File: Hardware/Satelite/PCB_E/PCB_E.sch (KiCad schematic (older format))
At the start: 15 parts, among them J1 Conn_02x02_Counter_Clockwise, J12 Conector_Expansion_CanSat, J14 Conn_01x06, J15 Conn_01x06, J2 Conn_02x02_Counter_Clockwise, J3 Conn_02x02_Counter_Clockwise, J4 Conn_02x10_Odd_Even, J5 Conn_02x10_Odd_Even, J6 Conn_02x10_Odd_Even, J7 Conn_02x10_Odd_Even, J8 Conn_01x04, M1 Spacer, M2 Spacer, M3 Spacer

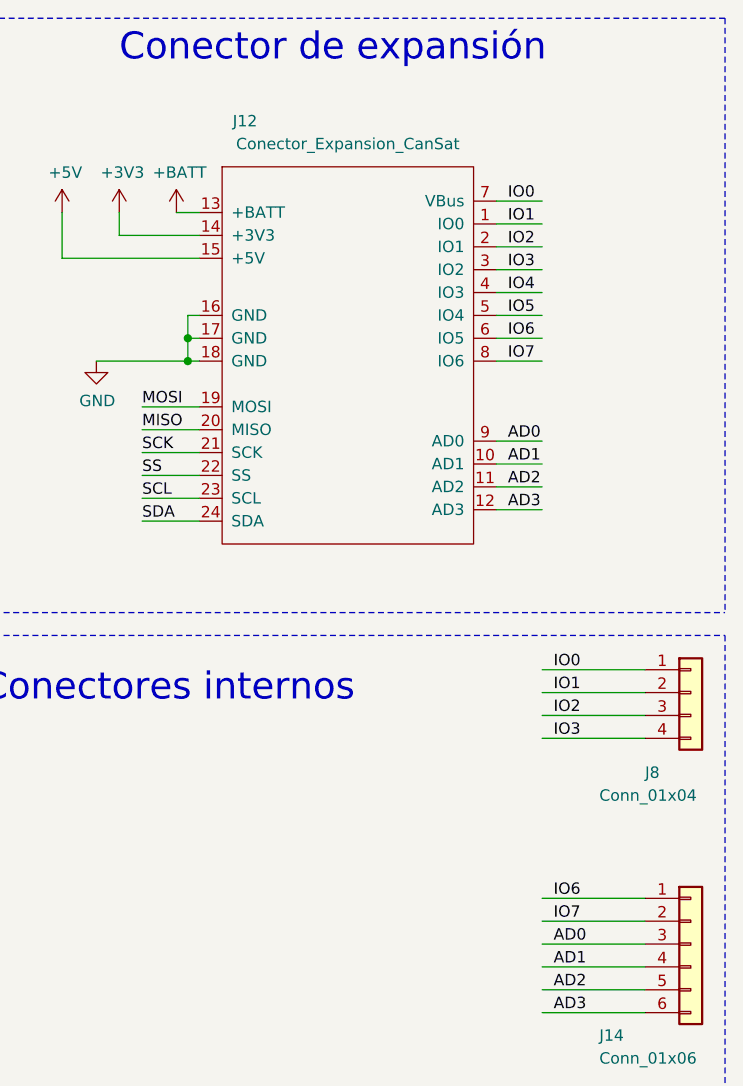
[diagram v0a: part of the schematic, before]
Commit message: Modificaciones D6 y serigrafia en PCB_E
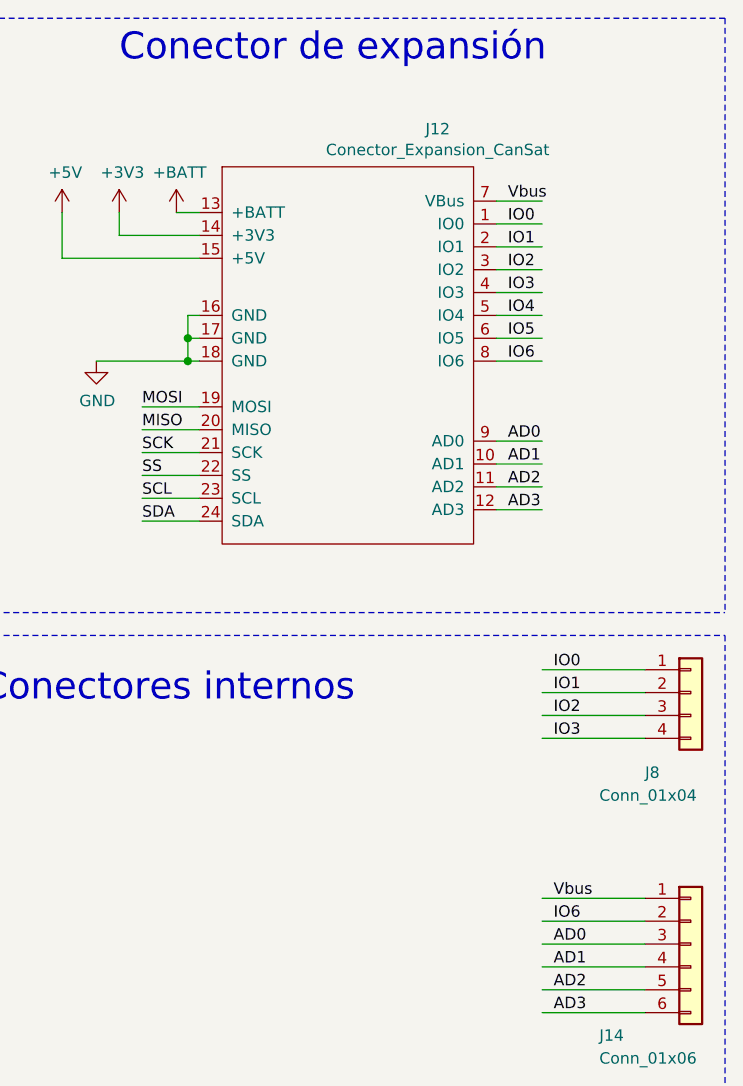
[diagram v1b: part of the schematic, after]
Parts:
- J12: Manufacturer Part Number SSQ-106-03-T-S -> (none); Quantity 4 -> (none)
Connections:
- net labels added: Vbus
- net labels removed: IO7
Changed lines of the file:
@@
 Text Label 9650 3900 0    50   ~ 0
 IO3
-Text Label 9450 2150 0    50   ~ 0
+Text Label 9450 2250 0    50   ~ 0
 IO6
 Wire Wire Line
@@
 Wire Wire Line
 	9600 5100 10050 5100
-Text Label 9450 2250 0    50   ~ 0
-IO7
+Text Label 9450 1550 0    50   ~ 0
+Vbus
 Text Label 9650 4800 0    50   ~ 0
 AD0
@@
 EndData
 $EndBitmap
-Text Label 9450 1550 0    50   ~ 0
+Text Label 9450 1650 0    50   ~ 0
 IO0
-Text Label 9450 1650 0    50   ~ 0
+Text Label 9450 1750 0    50   ~ 0
 IO1
-Text Label 9450 1750 0    50   ~ 0
+Text Label 9450 1850 0    50   ~ 0
 IO2
-Text Label 9450 1850 0    50   ~ 0
+Text Label 9450 1950 0    50   ~ 0
 IO3
-Text Label 9450 1950 0    50   ~ 0
+Text Label 9450 2050 0    50   ~ 0
 IO4
-Text Label 9450 2050 0    50   ~ 0
+Text Label 9450 2150 0    50   ~ 0
 IO5
 Text Label 9450 2600 0    50   ~ 0
@@
 Wire Wire Line
 	10050 4700 9600 4700
-Text Label 9650 4600 0    50   ~ 0
+Text Label 9650 4700 0    50   ~ 0
 IO6
-Text Label 9650 4700 0    50   ~ 0
-IO7
 $Comp
 L AXTEC_IC:MH_CanSat MH1
@@
 Text Notes 4450 4150 0    118  ~ 0
 Agujeros de montaje
-$Comp
-L AXTEC_IC:Conector_Expansion_CanSat J12
-U 1 1 5BC6ED70
-P 8750 2100
-F 0 "J12" H 8300 3000 50  0000 C CNN
-F 1 "Conector_Expansion_CanSat" H 8750 2900 50  0000 C CNN
-F 2 "AXTEC:Conector_Expansion_CanSat" H 8750 2600 50  0001 C CNN
-F 3 "" H 8750 2600 50  0001 C CNN
-F 4 "SSQ-106-03-T-S" H 8750 2100 50  0001 C CNN "Manufacturer Part Number"
-F 5 "4" H 8750 2100 50  0001 C CNN "Quantity"
-	1    8750 2100
-	1    0    0    -1
-$EndComp
 Wire Wire Line
 	8100 2950 7850 2950
@@
 	1    0    0    -1
 $EndComp
+$Comp
+L AXTEC_IC:Conector_Expansion_CanSat J12
+U 1 1 5C26BB39
+P 8750 2100
+F 0 "J12" H 9143 2965 50  0000 C CNN
+F 1 "Conector_Expansion_CanSat" H 9143 2874 50  0000 C CNN
+F 2 "AXTEC:Conector_Expansion_CanSat" H 8750 2600 50  0001 C CNN
+F 3 "" H 8750 2600 50  0001 C CNN
+	1    8750 2100
+	1    0    0    -1
+$EndComp
+Text Label 9650 4600 0    50   ~ 0
+Vbus
 $EndSCHEMATC

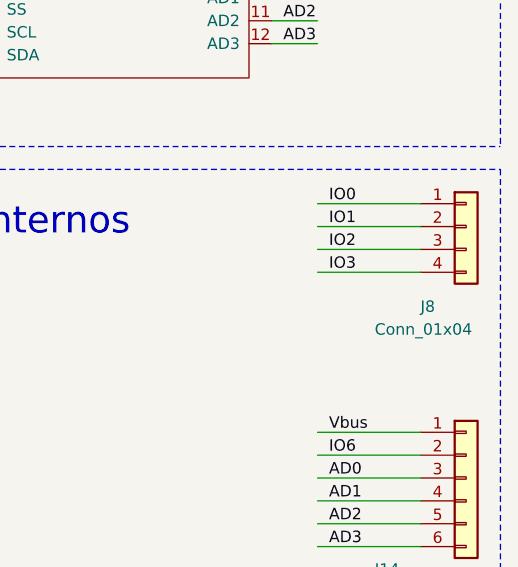
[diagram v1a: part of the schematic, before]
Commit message: Agregados pines faltantes en PCB_E
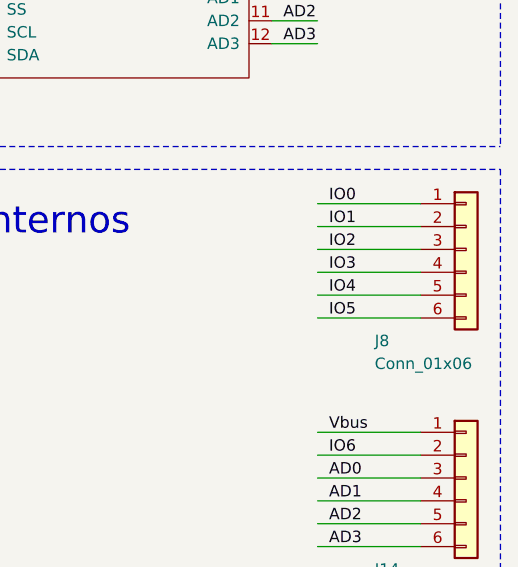
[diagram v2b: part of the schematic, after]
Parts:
- removed J8: Conn_01x04, Connector_PinHeader_2.54mm:PinHeader_1x04_P2.54mm_Vertical, symbol Connector_Generic:Conn_01x04
- added J8: Conn_01x06, Connector_PinHeader_2.54mm:PinHeader_1x06_P2.54mm_Vertical, symbol Connector_Generic:Conn_01x06
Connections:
- wire segments 75 -> 77
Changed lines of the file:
@@
-$EndComp
-$Comp
-L Connector_Generic:Conn_01x04 J8
-U 1 1 5BE3BD5B
-P 10250 3700
-F 0 "J8" H 10050 3350 50  0000 L CNN
-F 1 "Conn_01x04" H 9850 3250 50  0000 L CNN
-F 2 "Connector_PinHeader_2.54mm:PinHeader_1x04_P2.54mm_Vertical" H 10250 3700 50  0001 C CNN
-F 3 "~" H 10250 3700 50  0001 C CNN
-	1    10250 3700
-	1    0    0    -1
 $EndComp
 $Comp
@@
 Text Label 9650 4600 0    50   ~ 0
 Vbus
+$Comp
+L Connector_Generic:Conn_01x06 J8
+U 1 1 5C2A870C
+P 10250 3800
+F 0 "J8" H 9850 3400 50  0000 L CNN
+F 1 "Conn_01x06" H 9850 3300 50  0000 L CNN
+F 2 "Connector_PinHeader_2.54mm:PinHeader_1x06_P2.54mm_Vertical" H 10250 3800 50  0001 C CNN
+F 3 "https://www.mouser.com/datasheet/2/527/ssw_sm-1370305.pdf" H 10250 3800 50  0001 C CNN
+	1    10250 3800
+	1    0    0    -1
+$EndComp
+Text Label 9650 4000 0    50   ~ 0
+IO4
+Text Label 9650 4100 0    50   ~ 0
+IO5
+Wire Wire Line
+	10050 4000 9600 4000
+Wire Wire Line
+	10050 4100 9600 4100
 $EndSCHEMATC
